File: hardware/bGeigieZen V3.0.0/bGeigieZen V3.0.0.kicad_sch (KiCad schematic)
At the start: 14 parts, among them J1 M5 2x15 pin, J10 QI GND, J11 QI charger Plus, J2 Geiger IRover, J3 GPS, J4 Geiger Safepulse, J5 Extra support header, J6 Grove, J8 QI charger ground, J9 QI Plus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

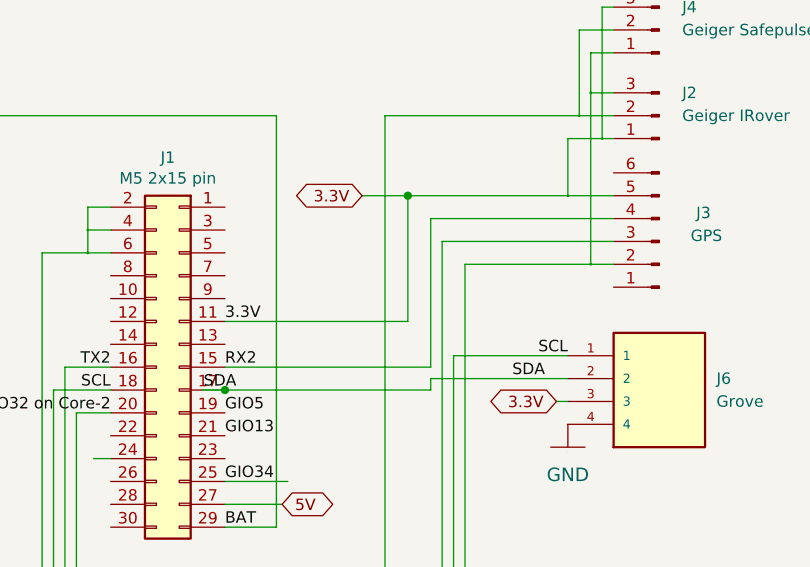
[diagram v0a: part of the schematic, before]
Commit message: added I2C to GPS bus . Louis idea.
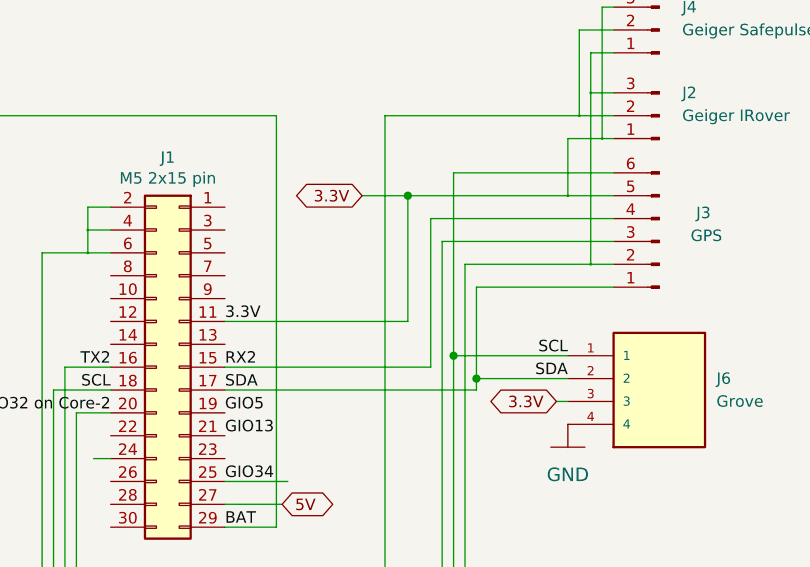
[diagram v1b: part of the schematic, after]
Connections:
- net SCL: now also J3.6 (Pin_6)
- net SDA: now also J3.1 (Pin_1)
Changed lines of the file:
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@@
   (junction (at 125.73 125.73) (diameter 0.3048) (color 0 0 0 0)
   )
-  (junction (at 146.05 96.52) (diameter 0) (color 0 0 0 0)
-  )
   (junction (at 186.69 82.55) (diameter 0.3048) (color 0 0 0 0)
   )
@@
   (junction (at 83.185 85.09) (diameter 0.3048) (color 0 0 0 0)
   )
+  (junction (at 173.99 95.25) (diameter 0) (color 0 0 0 0)
+  )
   (junction (at 186.69 63.5) (diameter 0.3048) (color 0 0 0 0)
   )
@@
   (junction (at 69.85 71.12) (diameter 0.3048) (color 0 0 0 0)
   )
+  (junction (at 171.45 92.71) (diameter 0) (color 0 0 0 0)
+  )
   (junction (at 184.15 74.93) (diameter 0.3048) (color 0 0 0 0)
   )
@@
     (stroke (width 0) (type default))
   )
+  (wire (pts (xy 189.23 72.39) (xy 171.45 72.39))
+    (stroke (width 0) (type default))
+  )
   (wire (pts (xy 74.295 85.09) (xy 83.185 85.09))
     (stroke (width 0) (type solid))
@@
     (stroke (width 0) (type solid))
   )
-  (wire (pts (xy 168.91 95.25) (xy 184.15 95.25))
-    (stroke (width 0) (type default))
-  )
   (wire (pts (xy 130.81 81.28) (xy 133.35 81.28))
     (stroke (width 0) (type solid))
@@
     (stroke (width 0) (type solid))
   )
-  (wire (pts (xy 146.05 96.52) (xy 168.91 96.52))
+  (wire (pts (xy 173.99 85.09) (xy 173.99 95.25))
     (stroke (width 0) (type default))
   )
@@
     (stroke (width 0) (type solid))
   )
+  (wire (pts (xy 146.05 96.52) (xy 173.99 96.52))
+    (stroke (width 0) (type default))
+  )
   (wire (pts (xy 130.81 78.74) (xy 130.81 76.2))
     (stroke (width 0) (type solid))
@@
     (stroke (width 0) (type solid))
   )
-  (wire (pts (xy 143.51 96.52) (xy 146.05 96.52))
-    (stroke (width 0) (type default))
-  )
   (wire (pts (xy 186.69 82.55) (xy 186.69 63.5))
     (stroke (width 0) (type solid))
@@
     (stroke (width 0) (type solid))
   )
+  (wire (pts (xy 189.23 85.09) (xy 173.99 85.09))
+    (stroke (width 0) (type default))
+  )
   (wire (pts (xy 69.85 77.47) (xy 69.85 80.01))
     (stroke (width 0) (type solid))
@@
     (stroke (width 0) (type solid))
   )
+  (wire (pts (xy 173.99 95.25) (xy 184.15 95.25))
+    (stroke (width 0) (type default))
+  )
   (wire (pts (xy 113.03 78.74) (xy 116.84 78.74))
     (stroke (width 0) (type solid))
@@
     (stroke (width 0) (type solid))
   )
-  (wire (pts (xy 168.91 95.25) (xy 168.91 96.52))
+  (wire (pts (xy 173.99 95.25) (xy 173.99 96.52))
     (stroke (width 0) (type default))
   )
@@
   (wire (pts (xy 186.69 63.5) (xy 186.69 59.055))
     (stroke (width 0) (type solid))
+  )
+  (wire (pts (xy 171.45 72.39) (xy 171.45 92.71))
+    (stroke (width 0) (type default))
   )
   (wire (pts (xy 166.37 74.93) (xy 166.37 88.9))
@@
     (effects (font (size 1.27 1.27) (color 56 88 62 1)) (justify left bottom))
   )
-  (label "SDA" (at 147.32 96.52 180) (fields_autoplaced)
-    (effects (font (size 1.27 1.27)) (justify right bottom))
+  (label "SDA" (at 146.05 96.52 0) (fields_autoplaced)
+    (effects (font (size 1.27 1.27)) (justify left bottom))
   )
   (label "TX2" (at 133.35 93.98 180) (fields_autoplaced)
@@
     (effects (font (size 1.27 1.27)) (justify left bottom))
   )
-  (label "SDA" (at 181.61 95.25 180) (fields_autoplaced)
-    (effects (font (size 1.27 1.27)) (justify right bottom))
-  )
+  (label "SDA" (at 184.15 95.25 180) (fields_autoplaced)
+    (effects (font (size 1.27 1.27)) (justify right bottom))
+  )

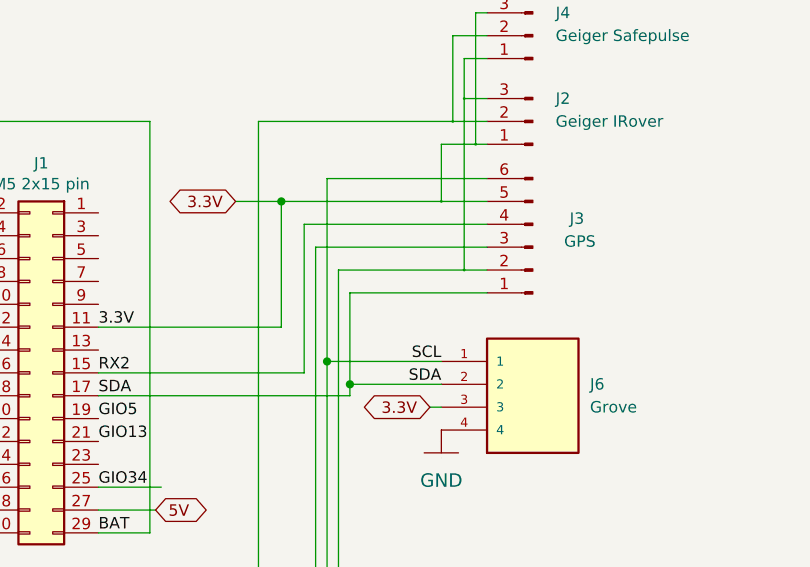
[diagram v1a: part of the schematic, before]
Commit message: Rolled back the I2C on the GPS
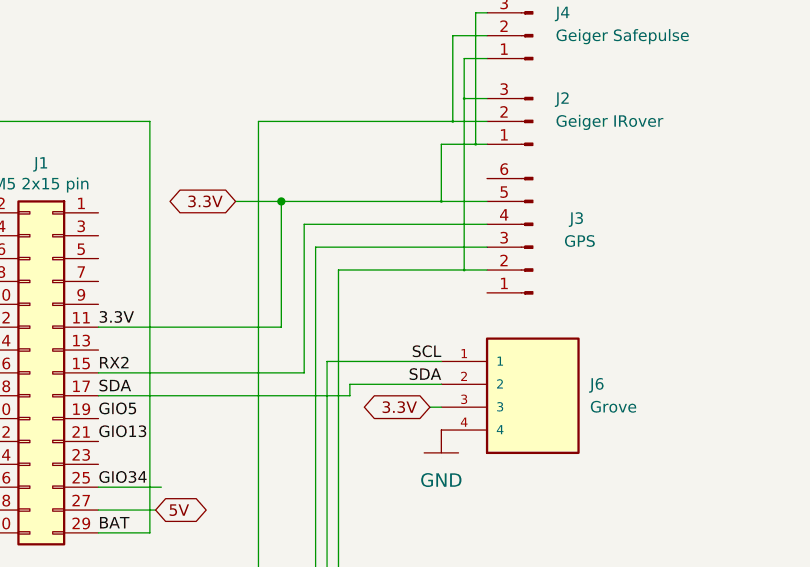
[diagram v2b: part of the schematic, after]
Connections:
- net SCL: no longer J3.6 (Pin_6)
- net SDA: no longer J3.1 (Pin_1)
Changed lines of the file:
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@@
   (junction (at 83.185 85.09) (diameter 0.3048) (color 0 0 0 0)
   )
-  (junction (at 173.99 95.25) (diameter 0) (color 0 0 0 0)
-  )
   (junction (at 186.69 63.5) (diameter 0.3048) (color 0 0 0 0)
   )
@@
   (junction (at 69.85 71.12) (diameter 0.3048) (color 0 0 0 0)
   )
-  (junction (at 171.45 92.71) (diameter 0) (color 0 0 0 0)
-  )
   (junction (at 184.15 74.93) (diameter 0.3048) (color 0 0 0 0)
   )
@@
     (stroke (width 0) (type default))
   )
-  (wire (pts (xy 189.23 72.39) (xy 171.45 72.39))
-    (stroke (width 0) (type default))
-  )
   (wire (pts (xy 74.295 85.09) (xy 83.185 85.09))
     (stroke (width 0) (type solid))
@@
     (stroke (width 0) (type solid))
   )
-  (wire (pts (xy 173.99 85.09) (xy 173.99 95.25))
-    (stroke (width 0) (type default))
-  )
   (wire (pts (xy 189.23 66.04) (xy 185.42 66.04))
     (stroke (width 0) (type solid))
@@
     (stroke (width 0) (type solid))
   )
-  (wire (pts (xy 189.23 85.09) (xy 173.99 85.09))
-    (stroke (width 0) (type default))
-  )
   (wire (pts (xy 69.85 77.47) (xy 69.85 80.01))
     (stroke (width 0) (type solid))
@@
     (stroke (width 0) (type solid))
   )
-  (wire (pts (xy 171.45 72.39) (xy 171.45 92.71))
-    (stroke (width 0) (type default))
-  )
   (wire (pts (xy 166.37 74.93) (xy 166.37 88.9))
